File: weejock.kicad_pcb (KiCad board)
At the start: 2 copper layers, 43 parts, among them J2 JST-PH2, K1 PG1350, K10 PG1350, K11 PG1350, K12 PG1350, K13 PG1350, K14 PG1350, K15 PG1350, K16 PG1350, K17 PG1350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

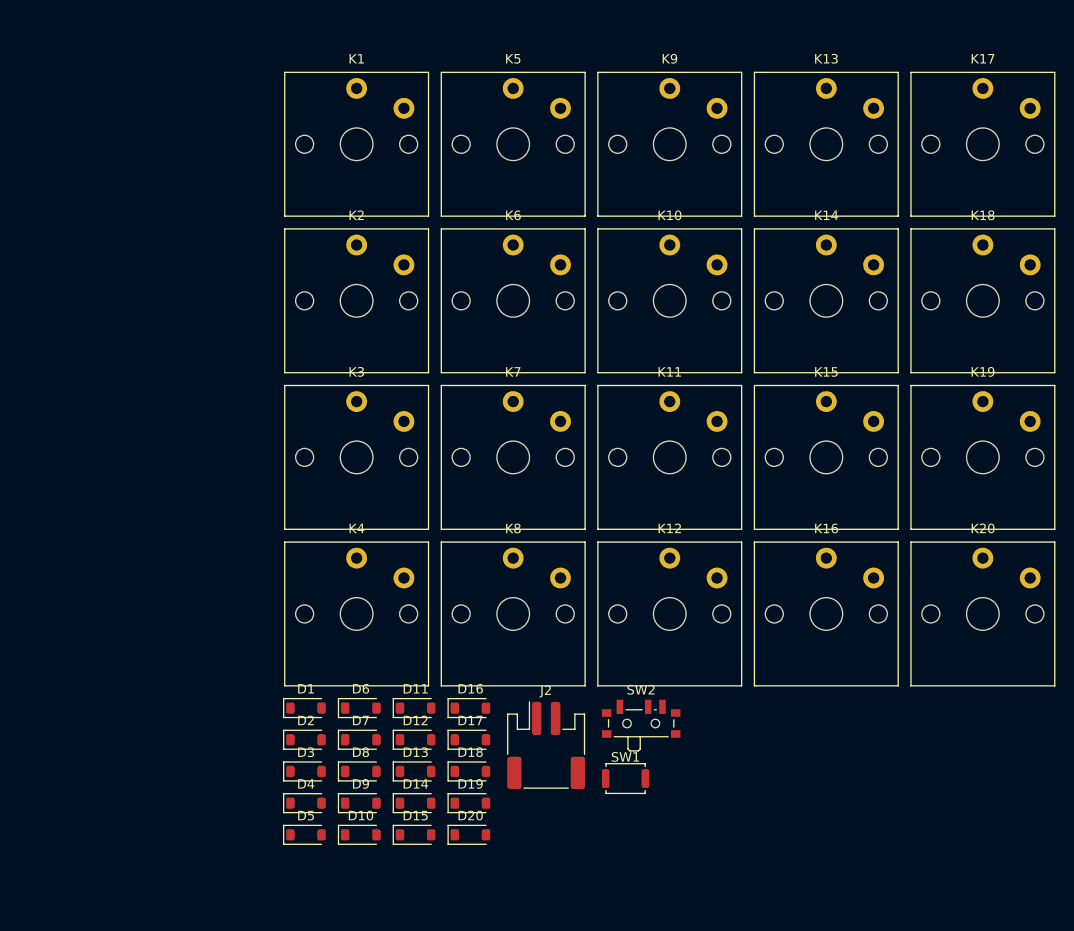
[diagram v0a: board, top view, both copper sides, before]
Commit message: Moving footprints around on the PCB layout.
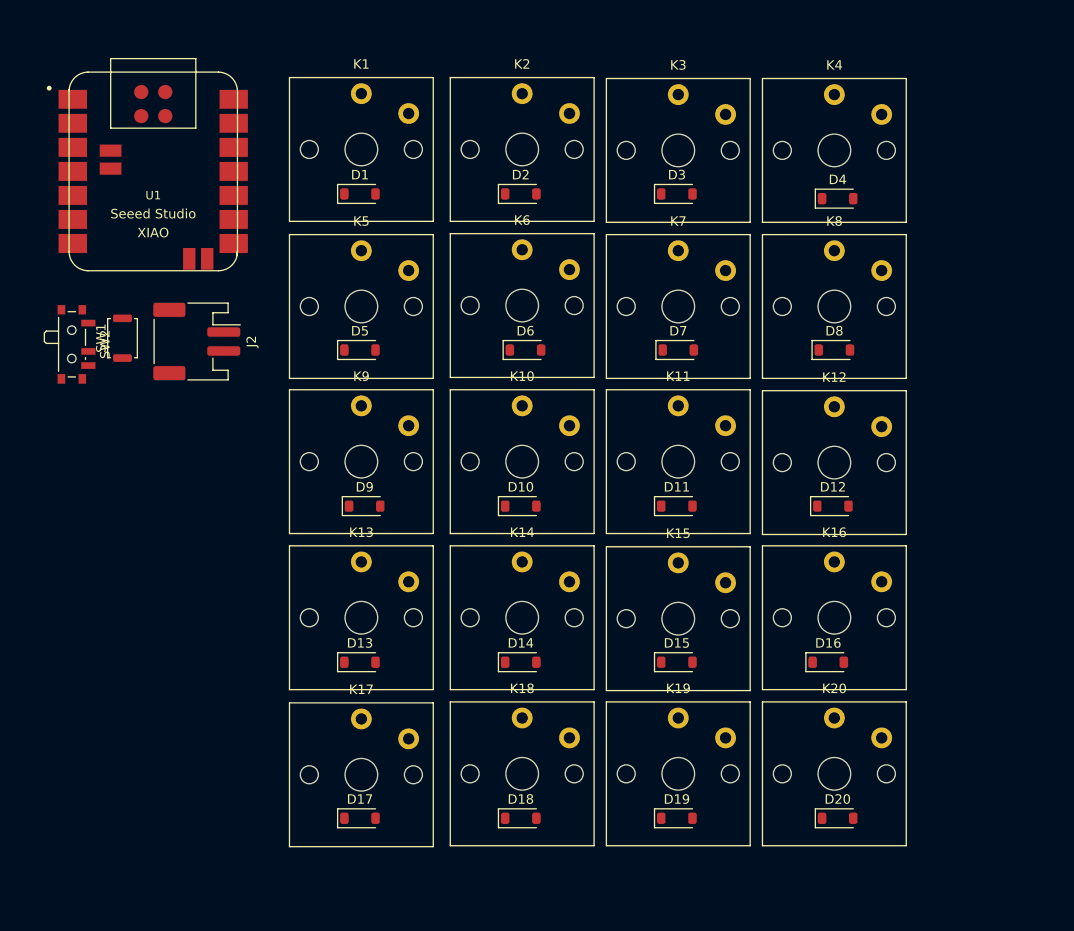
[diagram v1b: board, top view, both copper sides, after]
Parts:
- added U1: Seeed Studio XIAO nRF52840, Seeed Studio XIAO Series Library:XIAO-nRF52840-Sense-14P-2.54-21X17.8MM, F.Cu at (86.5, 60.6)
- moved K17 93.6 mm to (108.5, 124.4)
- moved D4 85.1 mm to (158.8, 63.5)
- moved D3 72.6 mm to (141.8, 63.0)
- moved SW2 71.9 mm to (78.2, 78.9), turned to -90 degrees
- moved SW1 70.7 mm to (83.2, 78.2), turned to 90 degrees
- moved K4 70.4 mm to (158.5, 58.4)
- moved K13 70.1 mm to (108.5, 107.8)
- moved K18 69.8 mm to (125.5, 124.3)
- moved D8 67.0 mm to (158.5, 79.5)
- moved D2 62.0 mm to (125.3, 63.0)
- moved J2 56.5 mm to (91.1, 78.6), turned to -90 degrees
- moved D1 54.6 mm to (108.3, 63.0)
- moved D7 53.1 mm to (142.0, 79.5)
- moved D5 51.6 mm to (108.3, 79.5)
- moved D12 50.6 mm to (158.3, 96.0)
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
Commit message: Routing traces.
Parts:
- moved K20 2.24 mm to (159.5, 126.3)
- moved D16 2.23 mm to (159.5, 114.0)
- moved D19 2.10 mm to (142.5, 131.0)
- moved D20 2.10 mm to (159.5, 131.0)
- moved K19 2.06 mm to (142.5, 126.3)
- moved D17 2.01 mm to (108.5, 131.0)
- moved D18 2.01 mm to (125.5, 131.0)
- moved K18 2.00 mm to (125.5, 126.3)
- moved K17 1.90 mm to (108.5, 126.3)
- moved K16 1.80 mm to (159.5, 109.3)
- moved D15 1.63 mm to (142.5, 114.0)
- moved D12 1.52 mm to (159.5, 97.0)
- moved D13 1.51 mm to (108.5, 114.0)
- moved D14 1.51 mm to (125.5, 114.0)
- moved K13 1.50 mm to (108.5, 109.3)
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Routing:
- net row4: track 0.00 -> 162.7 mm, vias 0 -> 2
- net col3: track 0.00 -> 161.9 mm, vias 0 -> 1
- net row3: track 0.00 -> 147.0 mm, vias 0 -> 2
- net col2: track 0.00 -> 146.8 mm, vias 0 -> 1
- net col1: track 0.00 -> 131.7 mm, vias 0 -> 1
- net row2: track 0.00 -> 131.4 mm, vias 0 -> 2
- net col0: track 0.00 -> 117.0 mm, vias 0 -> 1
- net row1: track 0.00 -> 115.8 mm, vias 0 -> 2
- net row0: track 0.00 -> 100.5 mm, vias 0 -> 2
- net GND: track 0.00 -> 55.5 mm
- net Net-(J2-Pin_1): track 0.00 -> 26.6 mm
- net RST: track 0.00 -> 23.0 mm
- net BAT+: track 0.00 -> 20.9 mm
- net Net-(D20-A): track 0.00 -> 9.89 mm
- net Net-(D19-A): track 0.00 -> 9.89 mm
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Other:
- board outline added: 95.4 x 89.7 mm

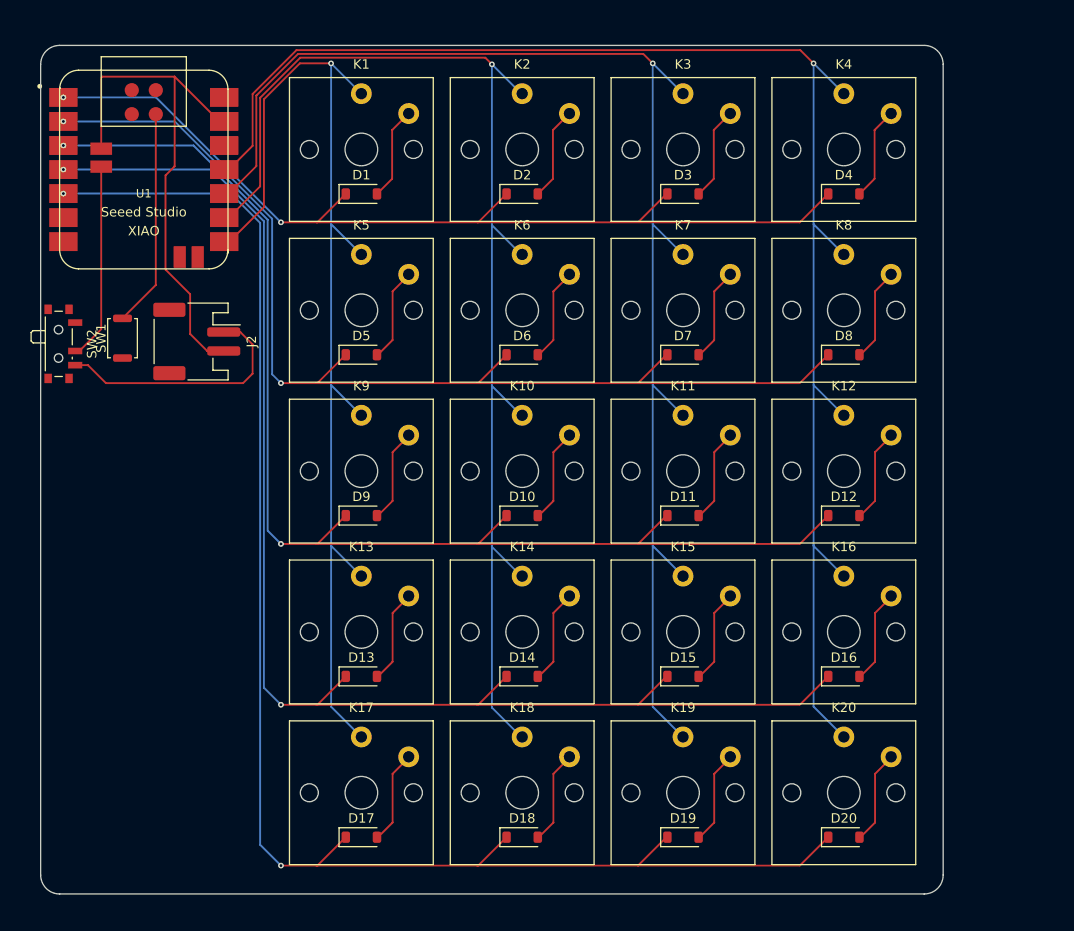
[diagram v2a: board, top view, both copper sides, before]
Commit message: Rerouting stuff to not be too near the edge of the board.
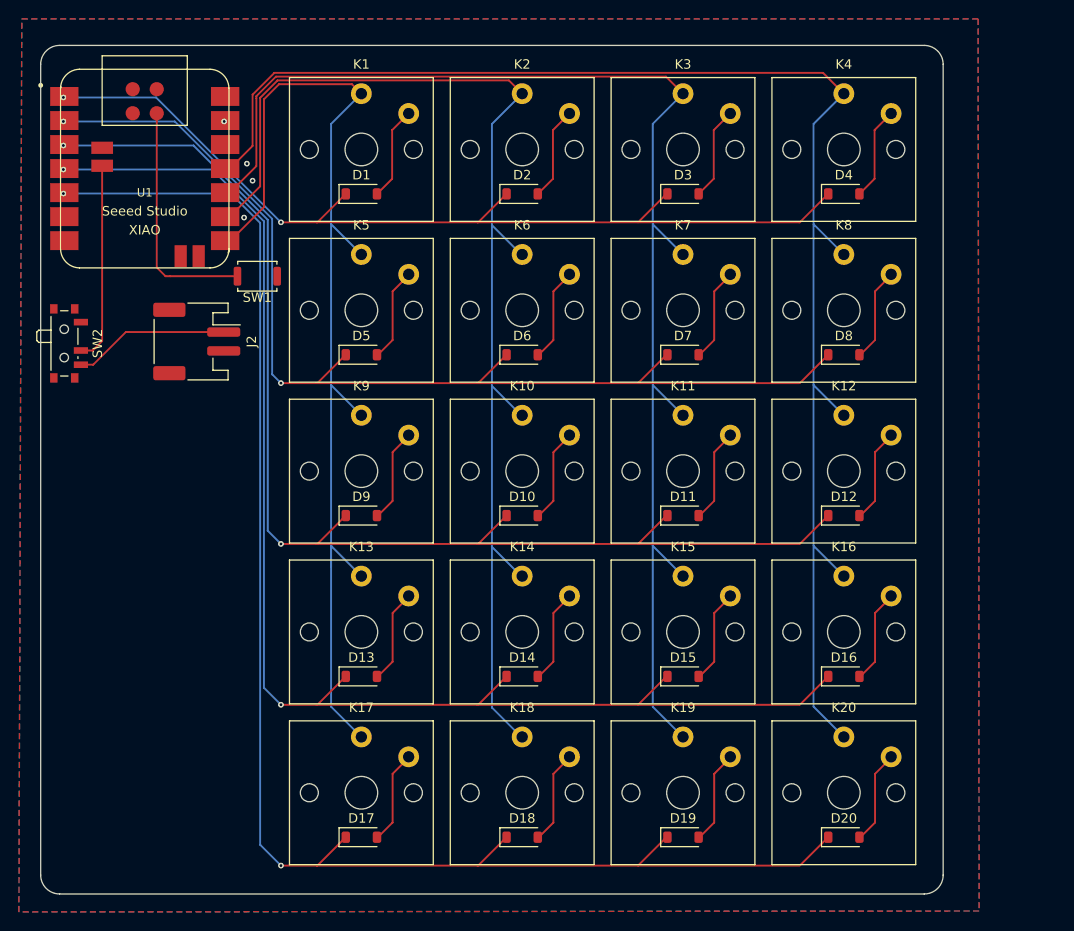
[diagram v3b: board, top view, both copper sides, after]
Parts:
- moved SW1 15.7 mm to (97.5, 71.7), turned to 180 degrees
- moved SW2 0.60 mm to (77.4, 78.8)
- moved U1 0.14 mm to (85.6, 60.3)
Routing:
- net GND: track 55.5 -> 0.50 mm, vias 0 -> 4
- net Net-(J2-Pin_1): track 26.6 -> 16.5 mm
- net col3: track 161.9 -> 158.0 mm, vias 1 -> 0
- net col1: track 131.7 -> 127.9 mm, vias 1 -> 0
- net col2: track 146.8 -> 143.0 mm, vias 1 -> 0
- net RST: track 23.0 -> 25.2 mm
- net col0: track 117.0 -> 115.6 mm, vias 1 -> 0
- net BAT+: track 20.9 -> 21.7 mm
- added copper zone on B.Cu, net GND
- added copper zone on F.Cu, net GND

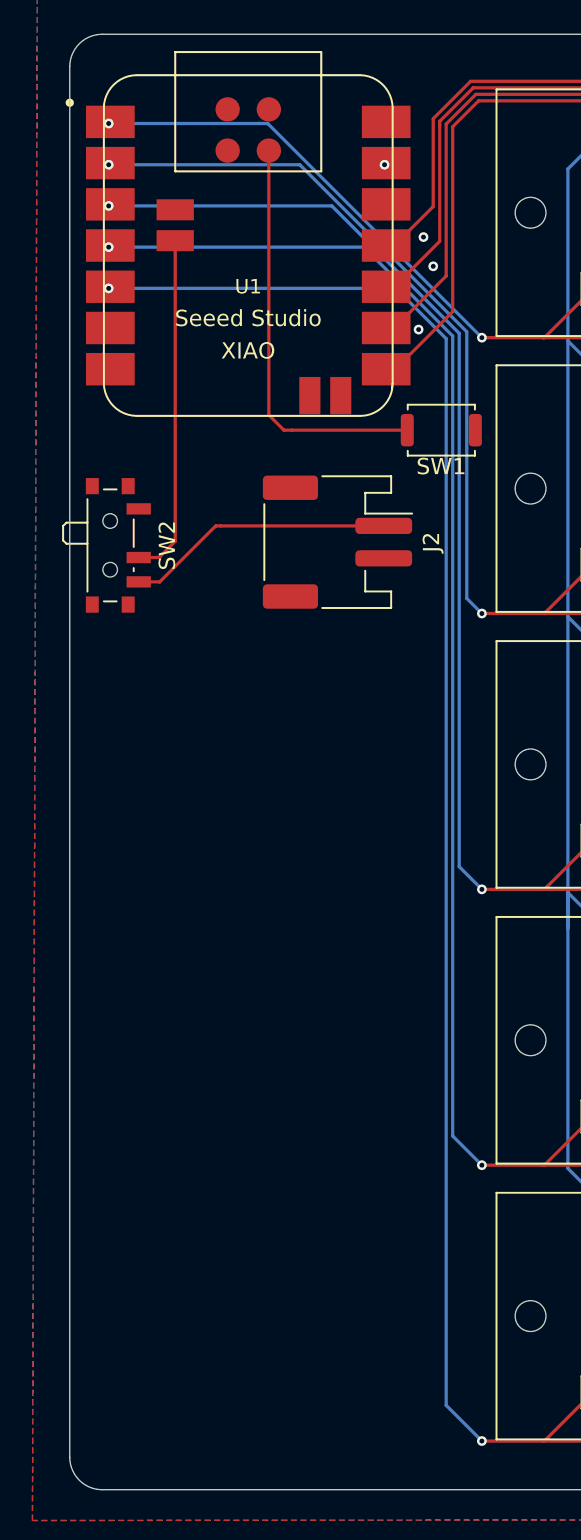
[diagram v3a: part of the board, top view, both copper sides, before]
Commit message: Perhaps misguided attempt to make hand-soldering holes for surface mount back pads.
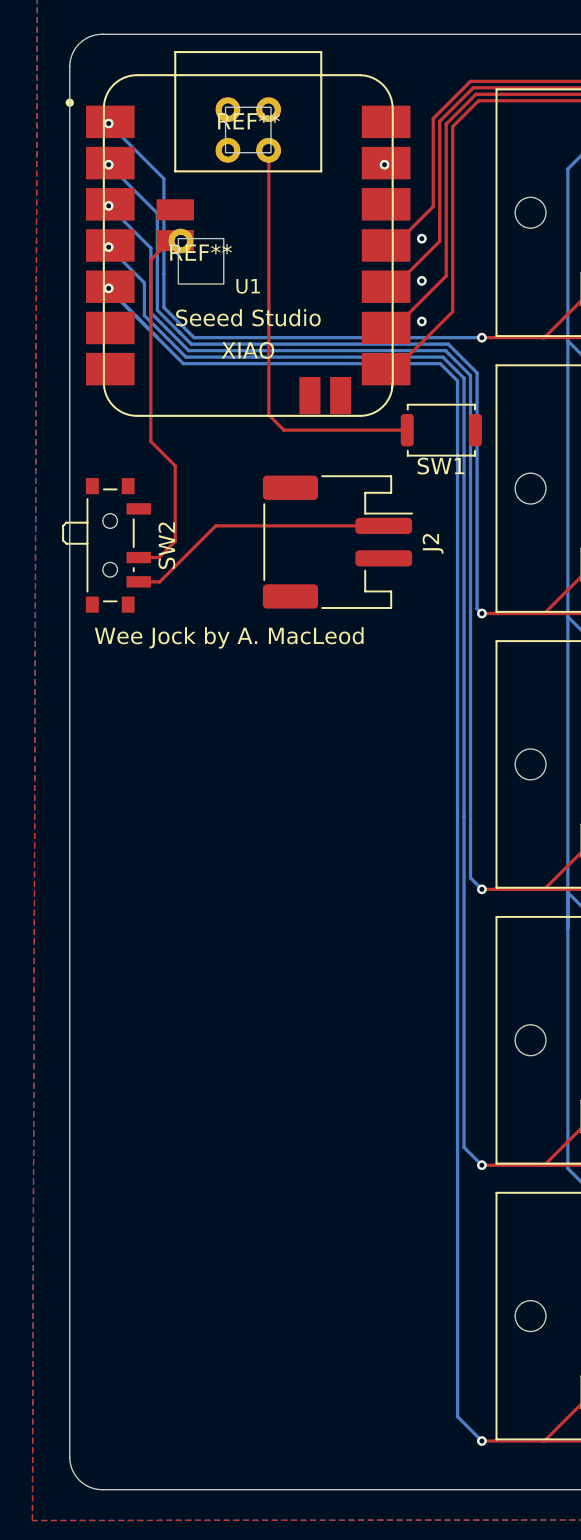
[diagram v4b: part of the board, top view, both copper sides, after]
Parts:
- added REF**: XIAO Clover Hole, weejock_library:XIAO Clover Hole, F.Cu at (85.6, 53.2)
- added REF**: XIAO Single Pad Clover Hole, weejock_library:XIAO Single Pad Clover Hole, F.Cu at (82.6, 61.3)
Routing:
- net row0: track 100.5 -> 105.1 mm
- net row4: track 162.7 -> 165.8 mm
- net row1: track 115.8 -> 118.3 mm
- net row2: track 131.4 -> 132.6 mm
- net BAT+: track 21.7 -> 22.6 mm
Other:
- board text added: "Wee Jock by A. MacLeod"

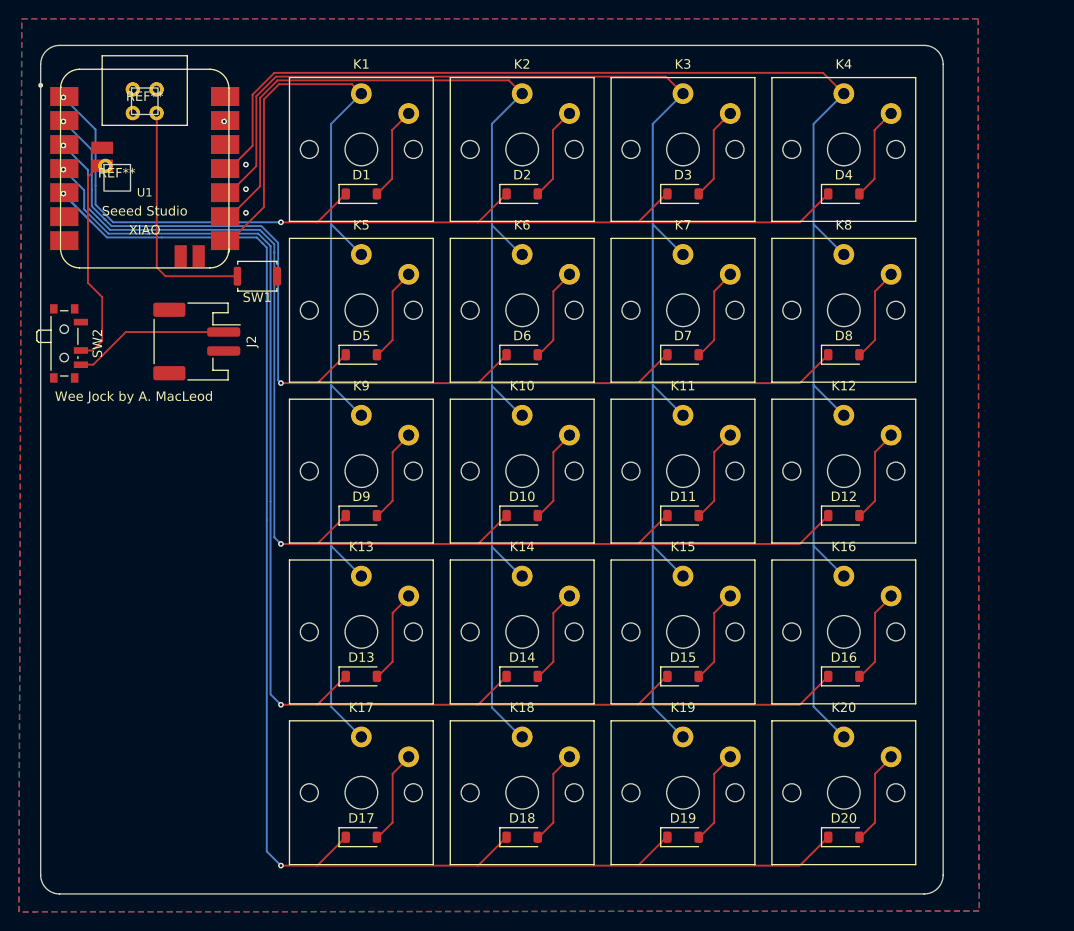
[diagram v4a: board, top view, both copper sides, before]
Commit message: Fixing up footprints for better routing and access around XIAO.
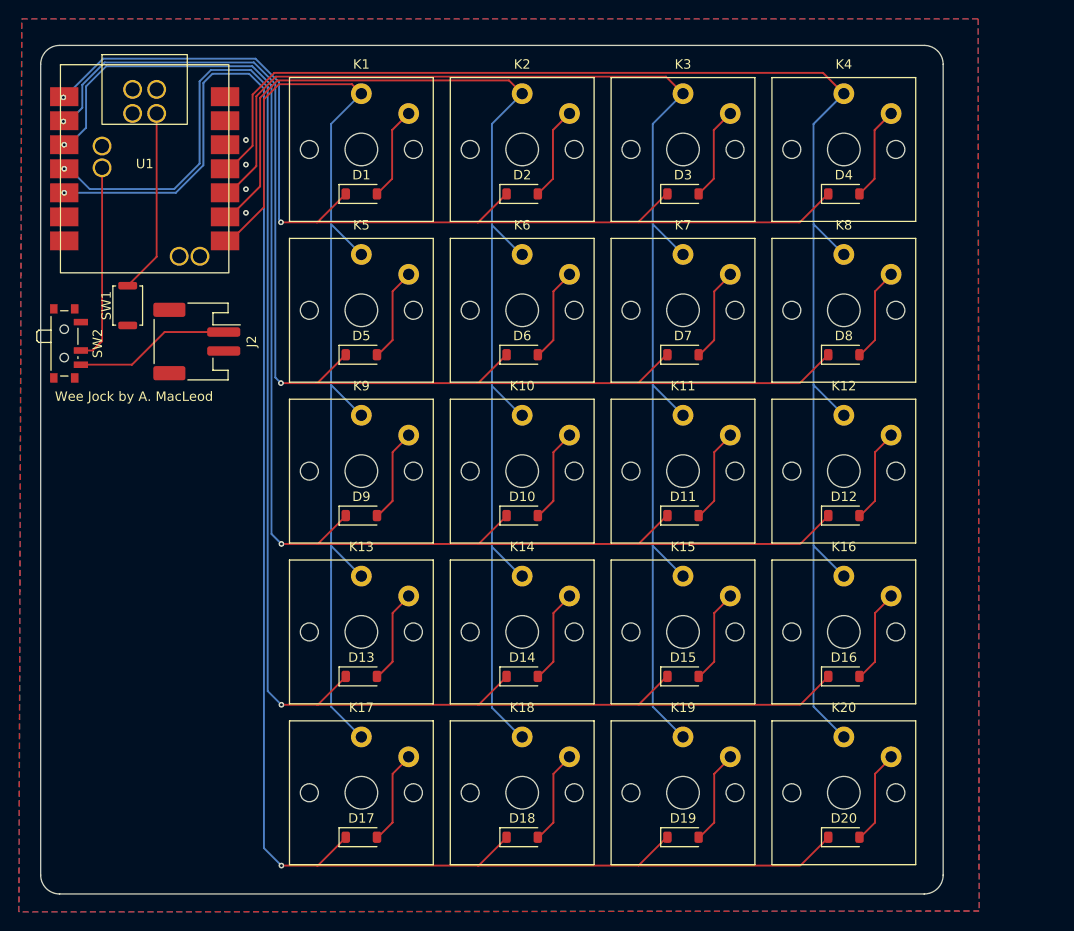
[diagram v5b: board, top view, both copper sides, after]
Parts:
- removed REF**: XIAO Clover Hole, weejock_library:XIAO Clover Hole
- removed REF**: XIAO Single Pad Clover Hole, weejock_library:XIAO Single Pad Clover Hole
- U1: footprint Seeed Studio XIAO Series Library:XIAO-nRF52840-Sense-14P-2.54-21X17.8MM -> weejock_library:Seeed XIAO Simplified
- moved SW1 14.0 mm to (83.8, 74.8), turned to 90 degrees
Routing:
- net row3: track 147.1 -> 171.6 mm
- net row4: track 165.8 -> 186.7 mm
- net row2: track 132.6 -> 149.4 mm
- net row1: track 118.3 -> 131.0 mm
- net row0: track 105.1 -> 112.4 mm
- net RST: track 25.2 -> 19.5 mm
- net BAT+: track 22.6 -> 22.0 mm
